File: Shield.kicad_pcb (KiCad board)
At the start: 2 copper layers, 54.6 x 53.6 mm, 33 parts, among them J1 Screw_Terminal_01x03, J2 Screw_Terminal_01x03, J3 Screw_Terminal_01x03, J4 Screw_Terminal_01x03, U1 MIC5219-3.3YM5, U2 MIC5219-3.3YM5, U3 MAX31865xTP, U4 MAX31865xTP, U5 MAX31865xTP, U6 MAX31865xTP

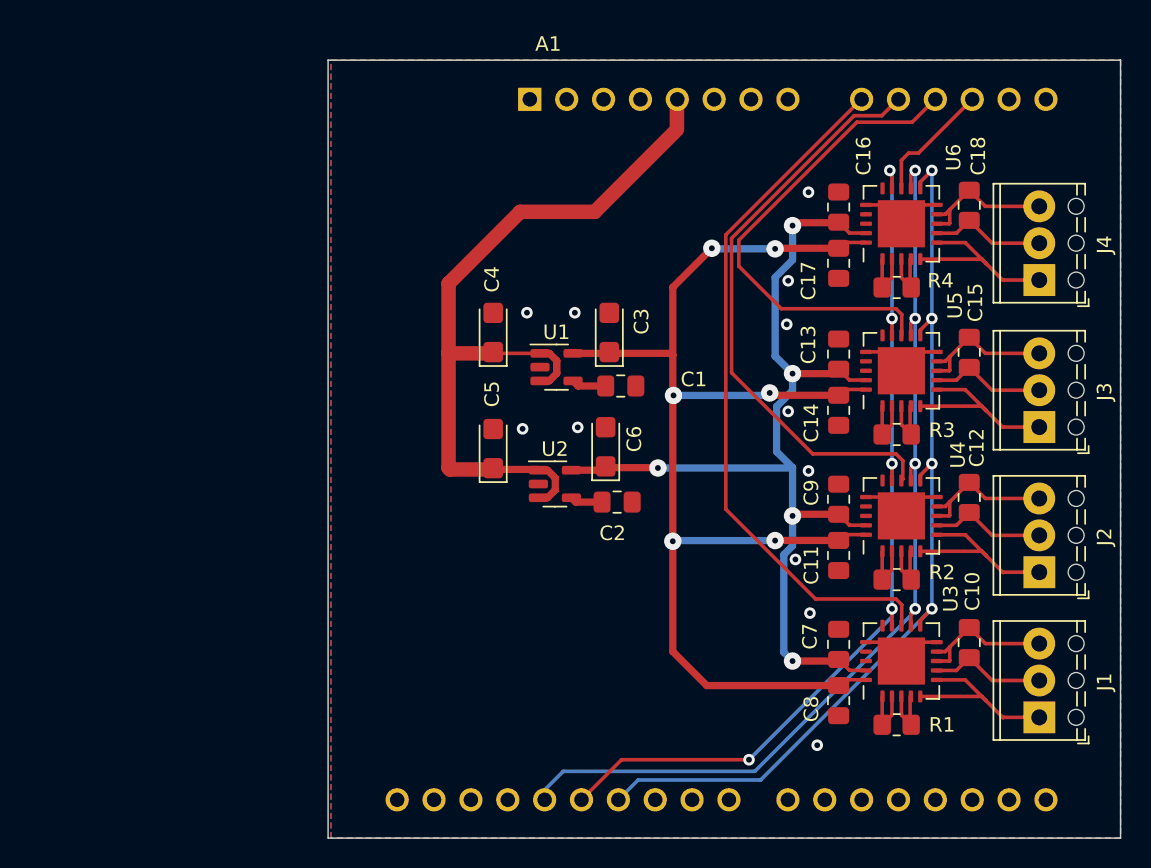
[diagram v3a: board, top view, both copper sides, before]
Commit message: Passe l'empreinte en TSOP
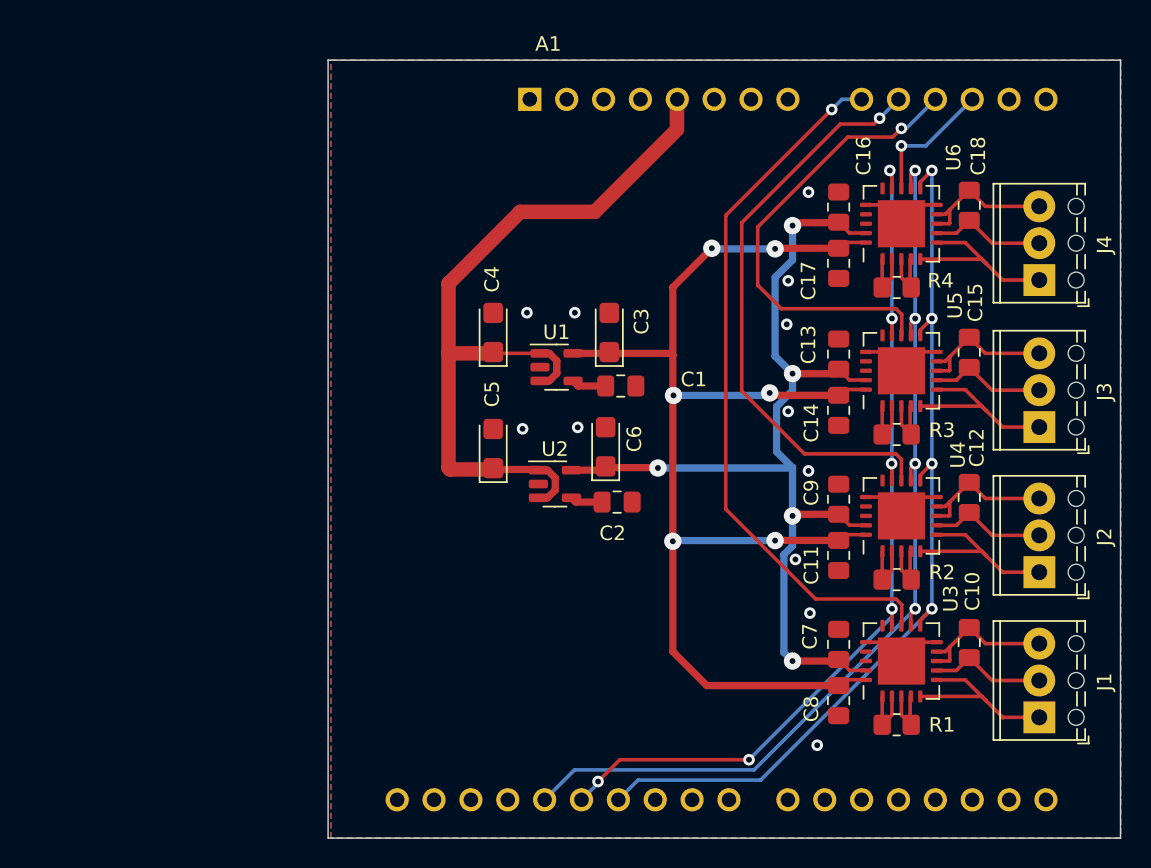
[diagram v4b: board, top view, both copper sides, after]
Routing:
- net /CS_MAX3: track 33.4 -> 32.1 mm, vias 0 -> 1
- net /CS_MAX1: track 48.4 -> 49.2 mm, vias 0 -> 1
- net /CS_MAX4: track 8.55 -> 9.14 mm, vias 0 -> 1
- net /SPI2_MISO: track 62.2 -> 62.3 mm, vias 5 -> 6
- net /CS_MAX2: track 40.4 -> 40.3 mm, vias 0 -> 1
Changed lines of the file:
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@@
   (via (at 133.2 77.9) (size 0.8) (drill 0.4) (layers "F.Cu" "B.Cu") (free) (net 2))
   (via (at 117 57.2) (size 0.8) (drill 0.4) (layers "F.Cu" "B.Cu") (free) (net 2))
-  (segment (start 139.525 77.320405) (end 139.525 78.7375) (width 0.25) (layer "F.Cu") (net 3))
-  (segment (start 127.4 51.835) (end 136.735 42.5) (width 0.25) (layer "F.Cu") (net 3))
-  (segment (start 127.4 70.73673) (end 133.58827 76.925) (width 0.25) (layer "F.Cu") (net 3))
-  (segment (start 127.4 51.835) (end 127.4 70.73673) (width 0.25) (layer "F.Cu") (net 3))
-  (segment (start 139.129595 76.925) (end 139.525 77.320405) (width 0.25) (layer "F.Cu") (net 3))
-  (segment (start 133.58827 76.925) (end 139.129595 76.925) (width 0.25) (layer "F.Cu") (net 3))
-  (segment (start 139.5 68.7625) (end 139.6 68.6625) (width 0.25) (layer "F.Cu") (net 4))
-  (segment (start 136.246396 43.625) (end 138.15 43.625) (width 0.25) (layer "F.Cu") (net 4))
-  (segment (start 127.8 61.33673) (end 127.8 52.071396) (width 0.25) (layer "F.Cu") (net 4))
-  (segment (start 133.38827 66.925) (end 127.8 61.33673) (width 0.25) (layer "F.Cu") (net 4))
-  (segment (start 139.6 68.6625) (end 139.6 67.395405) (width 0.25) (layer "F.Cu") (net 4))
-  (segment (start 139.129595 66.925) (end 133.38827 66.925) (width 0.25) (layer "F.Cu") (net 4))
-  (segment (start 127.8 52.071396) (end 136.246396 43.625) (width 0.25) (layer "F.Cu") (net 4))
-  (segment (start 138.15 43.625) (end 139.275 42.5) (width 0.25) (layer "F.Cu") (net 4))
-  (segment (start 139.6 67.395405) (end 139.129595 66.925) (width 0.25) (layer "F.Cu") (net 4))
-  (segment (start 140.24 44.075) (end 136.432792 44.075) (width 0.25) (layer "F.Cu") (net 5))
+  (segment (start 127.4 50.5) (end 134.699998 43.2) (width 0.25) (layer "F.Cu") (net 3))
+  (segment (start 139.525 77.320405) (end 139.129595 76.925) (width 0.25) (layer "F.Cu") (net 3))
+  (segment (start 133.58827 76.925) (end 127.4 70.73673) (width 0.25) (layer "F.Cu") (net 3))
+  (segment (start 139.129595 76.925) (end 133.58827 76.925) (width 0.25) (layer "F.Cu") (net 3))
+  (segment (start 139.525 78.7375) (end 139.525 77.320405) (width 0.25) (layer "F.Cu") (net 3))
+  (segment (start 127.4 70.73673) (end 127.4 50.5) (width 0.25) (layer "F.Cu") (net 3))
+  (via (at 134.699998 43.2) (size 0.8) (drill 0.4) (layers "F.Cu" "B.Cu") (net 3))
+  (segment (start 136.76 42.5) (end 135.399998 42.5) (width 0.25) (layer "B.Cu") (net 3))
+  (segment (start 135.399998 42.5) (end 134.699998 43.2) (width 0.25) (layer "B.Cu") (net 3))
+  (segment (start 128.5 51) (end 135.3 44.2) (width 0.25) (layer "F.Cu") (net 4))
+  (segment (start 139.5 68.7625) (end 139.5 67.295405) (width 0.25) (layer "F.Cu") (net 4))
+  (segment (start 137.6 44.2) (end 138 43.8) (width 0.25) (layer "F.Cu") (net 4))
+  (segment (start 139.129595 66.925) (end 132.825 66.925) (width 0.25) (layer "F.Cu") (net 4))
+  (segment (start 139.5 67.295405) (end 139.129595 66.925) (width 0.25) (layer "F.Cu") (net 4))
+  (segment (start 132.825 66.925) (end 128.5 62.6) (width 0.25) (layer "F.Cu") (net 4))
+  (segment (start 135.3 44.2) (end 137.6 44.2) (width 0.25) (layer "F.Cu") (net 4))
+  (segment (start 128.5 62.6) (end 128.5 51) (width 0.25) (layer "F.Cu") (net 4))
+  (via (at 138 43.8) (size 0.8) (drill 0.4) (layers "F.Cu" "B.Cu") (net 4))
+  (segment (start 139.3 42.5) (end 138 43.8) (width 0.25) (layer "B.Cu") (net 4))
+  (segment (start 139.5 44.5) (end 138.9 45.1) (width 0.25) (layer "F.Cu") (net 5))
+  (segment (start 135.8 45.1) (end 129.6 51.3) (width 0.25) (layer "F.Cu") (net 5))
   (segment (start 131.225 56.925) (end 139.129595 56.925) (width 0.25) (layer "F.Cu") (net 5))
-  (segment (start 128.3 52.2) (end 128.3 54) (width 0.25) (layer "F.Cu") (net 5))
-  (segment (start 135.5 45) (end 128.3 52.2) (width 0.25) (layer "F.Cu") (net 5))
+  (segment (start 129.6 55.3) (end 131.225 56.925) (width 0.25) (layer "F.Cu") (net 5))
+  (segment (start 129.6 51.3) (end 129.6 55.3) (width 0.25) (layer "F.Cu") (net 5))
+  (segment (start 139.525 57.320405) (end 139.525 58.7375) (width 0.25) (layer "F.Cu") (net 5))
   (segment (start 139.129595 56.925) (end 139.525 57.320405) (width 0.25) (layer "F.Cu") (net 5))
-  (segment (start 136.432792 44.075) (end 135.507792 45) (width 0.25) (layer "F.Cu") (net 5))
-  (segment (start 139.525 57.320405) (end 139.525 58.7375) (width 0.25) (layer "F.Cu") (net 5))
-  (segment (start 141.815 42.5) (end 140.24 44.075) (width 0.25) (layer "F.Cu") (net 5))
-  (segment (start 128.3 54) (end 131.225 56.925) (width 0.25) (layer "F.Cu") (net 5))
-  (segment (start 135.507792 45) (end 135.5 45) (width 0.25) (layer "F.Cu") (net 5))
-  (segment (start 140 46.2) (end 139.5 46.7) (width 0.25) (layer "F.Cu") (net 6))
-  (segment (start 144.38 42.5) (end 140.68 46.2) (width 0.25) (layer "F.Cu") (net 6))
-  (segment (start 139.5 46.7) (end 139.5 48.6335) (width 0.25) (layer "F.Cu") (net 6))
-  (segment (start 140.68 46.2) (end 140 46.2) (width 0.25) (layer "F.Cu") (net 6))
+  (segment (start 138.9 45.1) (end 135.8 45.1) (width 0.25) (layer "F.Cu") (net 5))
+  (via (at 139.5 44.5) (size 0.8) (drill 0.4) (layers "F.Cu" "B.Cu") (net 5))
+  (segment (start 141.84 42.5) (end 139.84 44.5) (width 0.25) (layer "B.Cu") (net 5))
+  (segment (start 139.84 44.5) (end 139.5 44.5) (width 0.25) (layer "B.Cu") (net 5))
+  (segment (start 139.5 45.7) (end 139.5 48.6335) (width 0.25) (layer "F.Cu") (net 6))
+  (via (at 139.5 45.7) (size 0.8) (drill 0.4) (layers "F.Cu" "B.Cu") (net 6))
+  (segment (start 144.38 42.5) (end 141.18 45.7) (width 0.25) (layer "B.Cu") (net 6))
+  (segment (start 141.18 45.7) (end 139.5 45.7) (width 0.25) (layer "B.Cu") (net 6))
   (segment (start 140.8 68.7625) (end 140.8 68.4) (width 0.25) (layer "F.Cu") (net 7))
   (segment (start 140.8 58.7625) (end 140.8 58.4) (width 0.25) (layer "F.Cu") (net 7))
@@
   (segment (start 141.6 47.4) (end 141.6 57.6) (width 0.25) (layer "B.Cu") (net 7))
   (segment (start 141.6 77.6) (end 129.8 89.4) (width 0.25) (layer "B.Cu") (net 7))
-  (segment (start 117.46 90.76) (end 120.22 88) (width 0.25) (layer "F.Cu") (net 8))
-  (segment (start 120.22 88) (end 129 88) (width 0.25) (layer "F.Cu") (net 8))
+  (segment (start 138.85 67.6245) (end 138.8255 67.6) (width 0.25) (layer "F.Cu") (net 8))
+  (segment (start 129 88) (end 120.1 88) (width 0.25) (layer "F.Cu") (net 8))
   (segment (start 138.85 47.55) (end 138.7 47.4) (width 0.25) (layer "F.Cu") (net 8))
   (segment (start 138.85 77.6) (end 138.85 78.7625) (width 0.25) (layer "F.Cu") (net 8))
   (segment (start 138.85 58.7625) (end 138.85 57.6) (width 0.25) (layer "F.Cu") (net 8))
-  (segment (start 138.85 68.7625) (end 138.85 67.6) (width 0.25) (layer "F.Cu") (net 8))
+  (segment (start 120.1 88) (end 118.6 89.5) (width 0.25) (layer "F.Cu") (net 8))
   (segment (start 138.85 48.6335) (end 138.85 47.55) (width 0.25) (layer "F.Cu") (net 8))
+  (segment (start 138.85 68.7625) (end 138.85 67.6245) (width 0.25) (layer "F.Cu") (net 8))
   (via (at 129 88) (size 0.8) (drill 0.4) (layers "F.Cu" "B.Cu") (net 8))
-  (via (at 138.85 67.6) (size 0.8) (drill 0.4) (layers "F.Cu" "B.Cu") (net 8))
+  (via (at 138.8255 67.6) (size 0.8) (drill 0.4) (layers "F.Cu" "B.Cu") (net 8))
   (via (at 138.85 57.6) (size 0.8) (drill 0.4) (layers "F.Cu" "B.Cu") (net 8))
   (via (at 138.7 47.4) (size 0.8) (drill 0.4) (layers "F.Cu" "B.Cu") (net 8))
+  (via (at 118.6 89.5) (size 0.8) (drill 0.4) (layers "F.Cu" "B.Cu") (net 8))
   (via (at 138.85 77.6) (size 0.8) (drill 0.4) (layers "F.Cu" "B.Cu") (net 8))
   (segment (start 138.85 78.15) (end 138.85 77.6) (width 0.25) (layer "B.Cu") (net 8))
   (segment (start 138.85 47.55) (end 138.7 47.4) (width 0.25) (layer "B.Cu") (net 8))
   (segment (start 129 88) (end 138.85 78.15) (width 0.25) (layer "B.Cu") (net 8))
-  (segment (start 138.85 77.6) (end 138.85 67.6) (width 0.25) (layer "B.Cu") (net 8))
+  (segment (start 117.46 90.76) (end 118.6 89.62) (width 0.25) (layer "B.Cu") (net 8))
+  (segment (start 138.85 57.6) (end 138.85 67.5755) (width 0.25) (layer "B.Cu") (net 8))
+  (segment (start 138.85 77.6) (end 138.85 67.6245) (width 0.25) (layer "B.Cu") (net 8))
+  (segment (start 138.85 67.6245) (end 138.8255 67.6) (width 0.25) (layer "B.Cu") (net 8))
+  (segment (start 118.6 89.62) (end 118.6 89.5) (width 0.25) (layer "B.Cu") (net 8))
   (segment (start 138.85 57.6) (end 138.85 47.55) (width 0.25) (layer "B.Cu") (net 8))
-  (segment (start 138.85 67.6) (end 138.85 57.6) (width 0.25) (layer "B.Cu") (net 8))
+  (segment (start 138.85 67.5755) (end 138.8255 67.6) (width 0.25) (layer "B.Cu") (net 8))
   (segment (start 140.15 77.9) (end 140.15 78.7625) (width 0.25) (layer "F.Cu") (net 9))
   (segment (start 140.15 58.7625) (end 140.15 57.9) (width 0.25) (layer "F.Cu") (net 9))
@@
   (segment (start 140.45 67.6) (end 140.45 77.6) (width 0.25) (layer "B.Cu") (net 9))
   (segment (start 140.45 57.6) (end 140.45 67.6) (width 0.25) (layer "B.Cu") (net 9))
-  (segment (start 129.4 88.8) (end 116.2 88.8) (width 0.25) (layer "B.Cu") (net 9))
-  (segment (start 116.2 88.8) (end 114.92 90.08) (width 0.25) (layer "B.Cu") (net 9))
-  (segment (start 140.45 77.75) (end 129.4 88.8) (width 0.25) (layer "B.Cu") (net 9))
-  (segment (start 140.45 77.6) (end 140.45 77.75) (width 0.25) (layer "B.Cu") (net 9))
+  (segment (start 129.349501 88.700499) (end 116.979501 88.700499) (width 0.25) (layer "B.Cu") (net 9))
+  (segment (start 116.979501 88.700499) (end 114.92 90.76) (width 0.25) (layer "B.Cu") (net 9))
   (segment (start 140.45 47.4) (end 140.45 57.6) (width 0.25) (layer "B.Cu") (net 9))
-  (segment (start 114.92 90.08) (end 114.92 90.76) (width 0.25) (layer "B.Cu") (net 9))
+  (segment (start 140.45 77.6) (end 129.349501 88.700499) (width 0.25) (layer "B.Cu") (net 9))
   (segment (start 117.225 62.25) (end 116.875 61.9) (width 0.5) (layer "F.Cu") (net 10))
   (segment (start 119.125 62.25) (end 117.225 62.25) (width 0.5) (layer "F.Cu") (net 10))

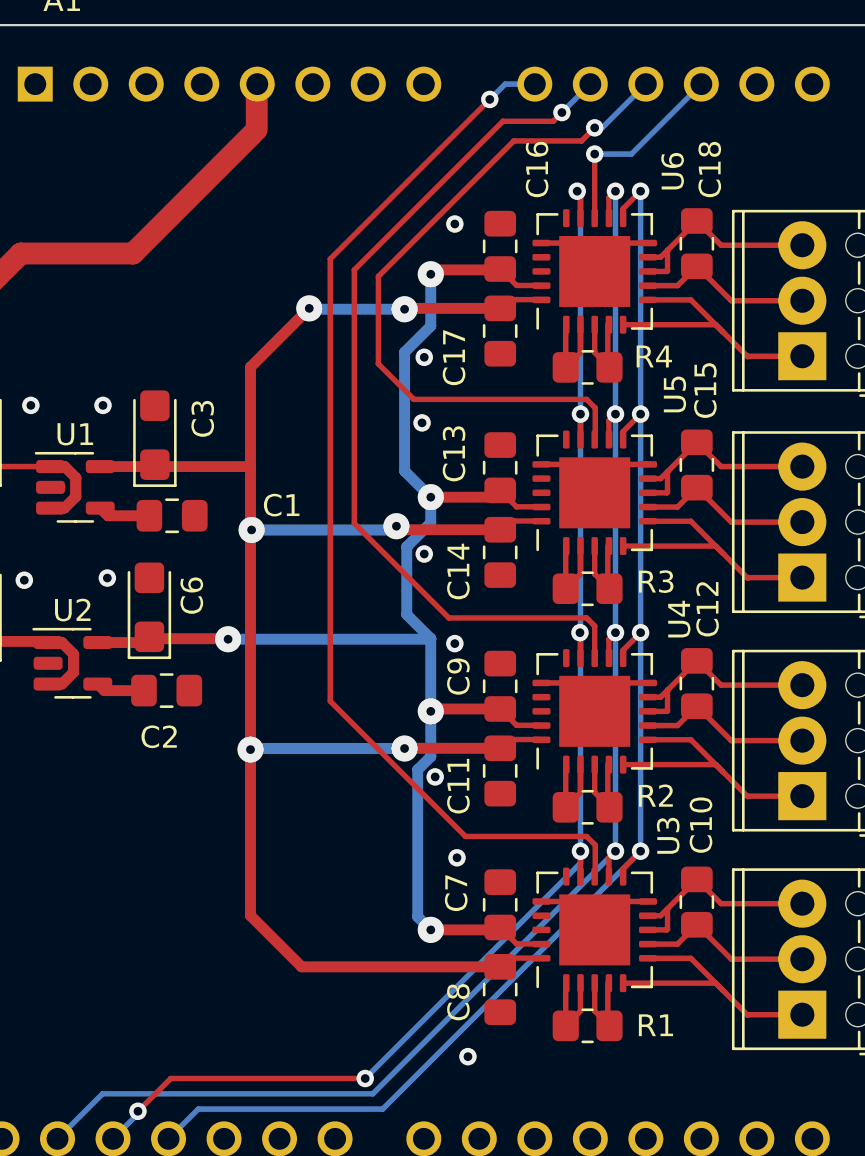
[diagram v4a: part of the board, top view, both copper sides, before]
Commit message: Passe certaine empreinte en 0603
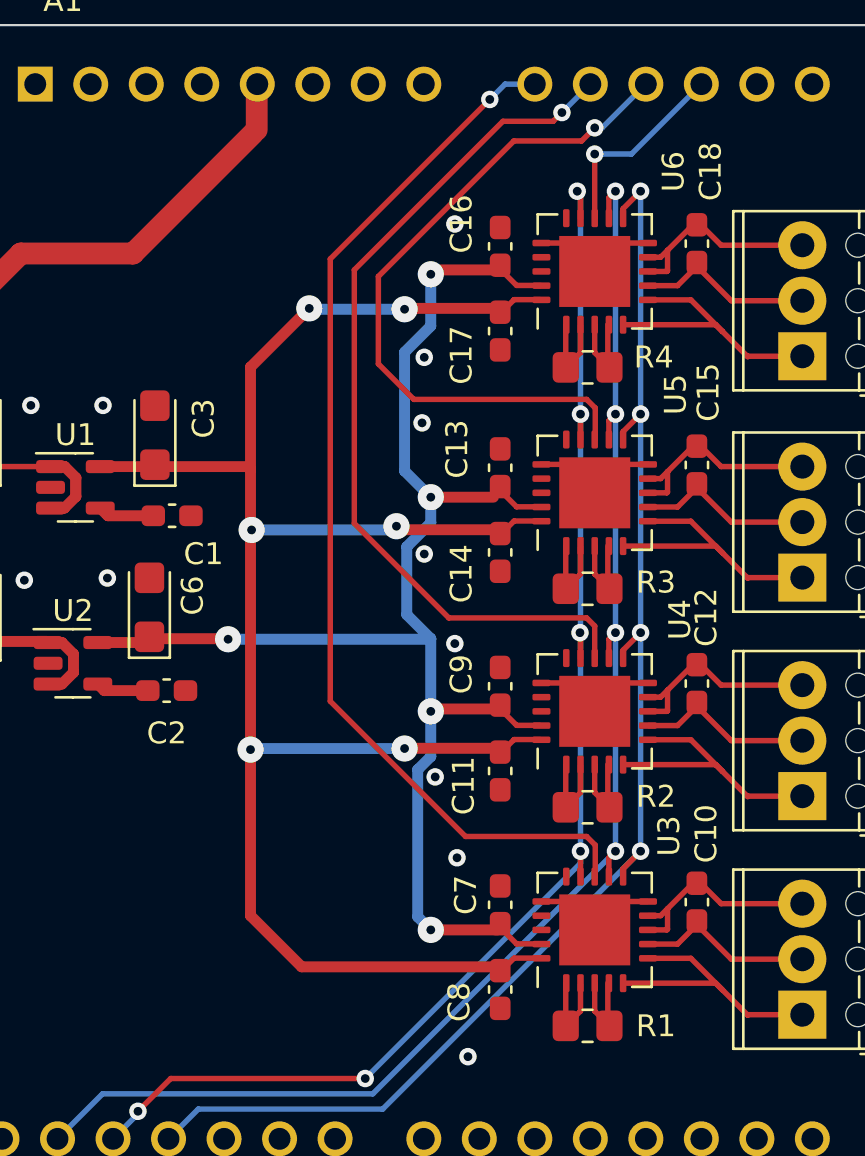
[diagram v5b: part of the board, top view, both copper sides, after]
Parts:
- C1, C10, C11, C12, C13, C14, C15, C16, C17, C18, C2, C7, C8, C9: footprint Capacitor_SMD:C_0805_2012Metric_Pad1.18x1.45mm_HandSolder -> Capacitor_SMD:C_0603_1608Metric_Pad1.08x0.95mm_HandSolder

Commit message: Passe les resistance 400 ohm en 1206
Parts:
- R1, R2, R3, R4: footprint Resistor_SMD:R_0805_2012Metric_Pad1.20x1.40mm_HandSolder -> Resistor_SMD:R_1206_3216Metric_Pad1.30x1.75mm_HandSolder
